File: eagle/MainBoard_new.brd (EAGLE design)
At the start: 62 parts, among them T1 BC847, U1 STM32F10XRXT6, U2 MPL115A, Y1 8MHz, Y2 32.768kHz

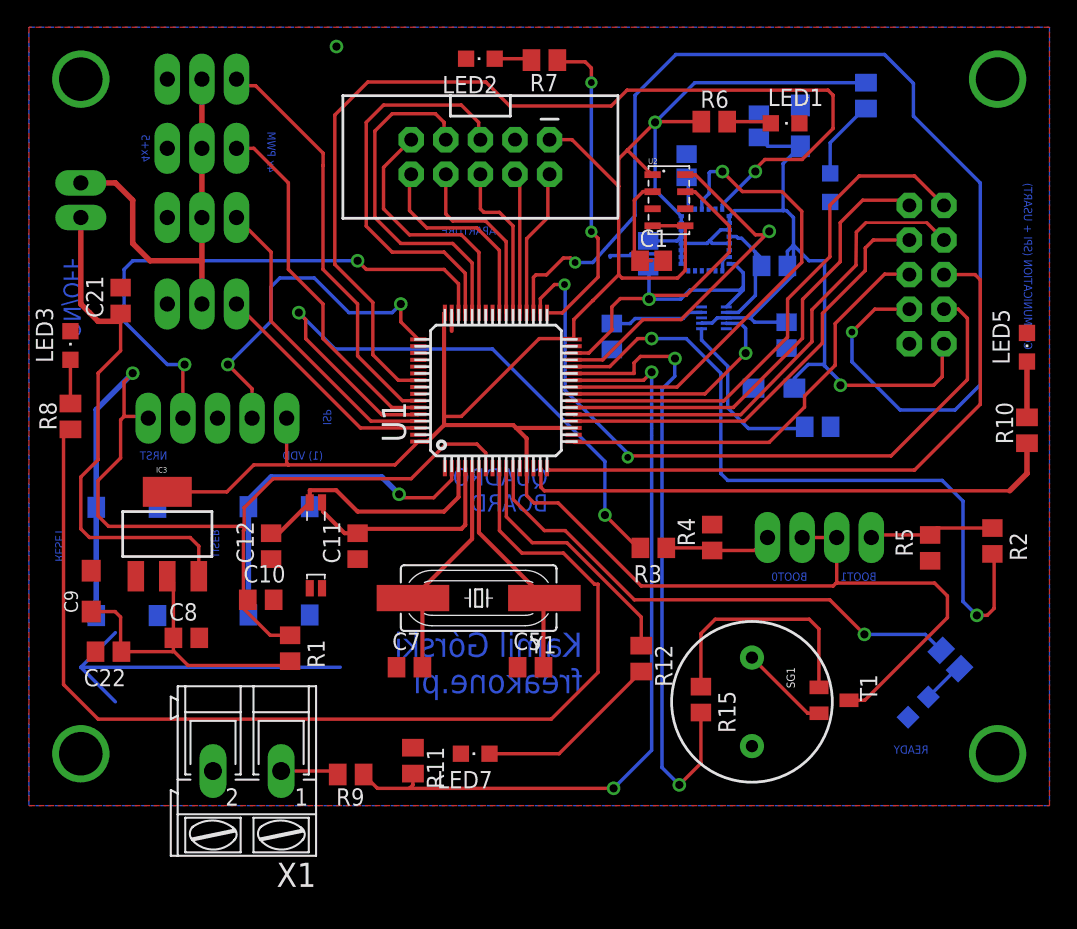
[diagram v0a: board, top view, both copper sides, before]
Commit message: likwidacja zbetnych przelotek do satlandu
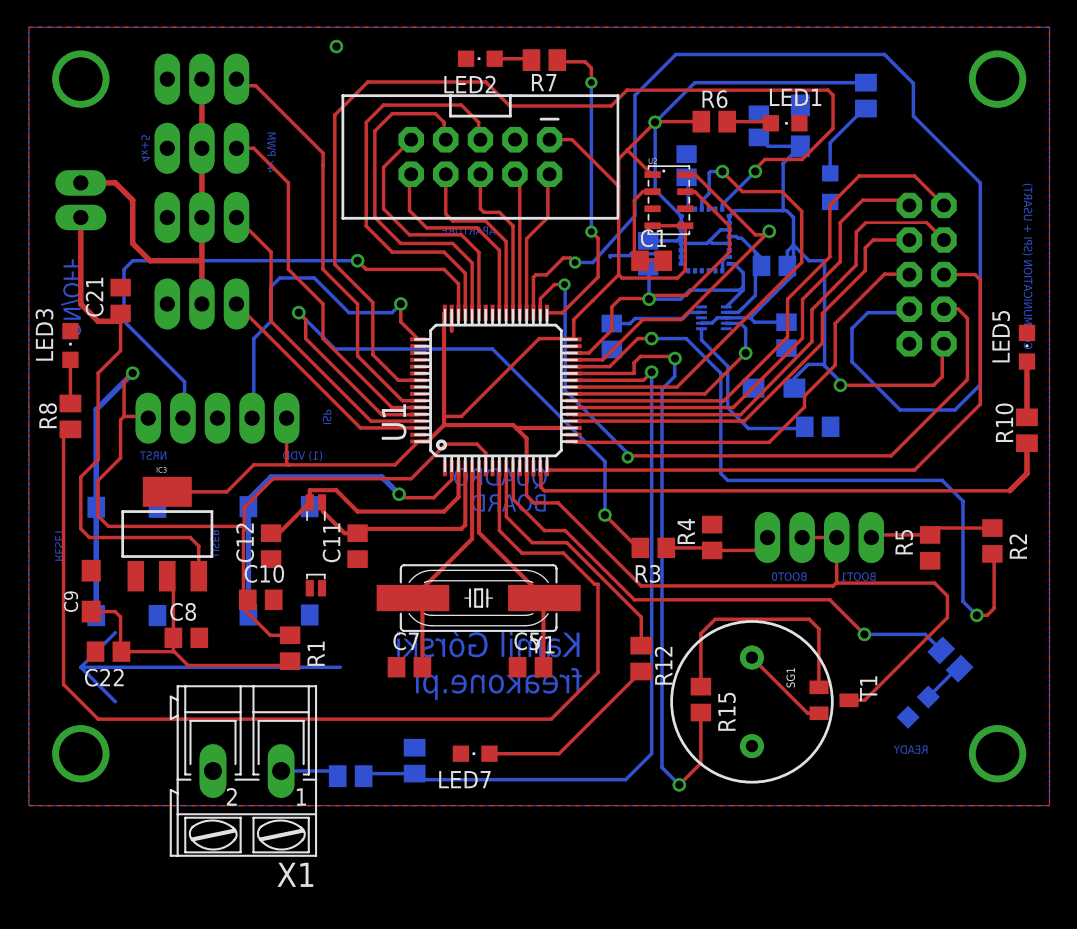
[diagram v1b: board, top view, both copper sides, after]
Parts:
- moved R11 0.13 mm to (18.2, 5.84), flipped to the bottom
- moved R9 0.13 mm to (13.5, 4.70), flipped to the bottom, turned to 0 degrees
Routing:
- net LIPO: track 57.7 -> 56.2 mm, vias 2 -> 1
- net SWCLK: track 25.9 -> 24.5 mm, vias 2 -> 1
- net SWDIO: track 41.2 -> 40.5 mm, vias 2 -> 1
- net OUT1: track 86.6 -> 86.8 mm, vias 2 -> 1
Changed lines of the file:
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@@
 <attribute name="OC_FARNELL" value="unknown" x="5.842" y="5.08" size="1.778" layer="27" rot="R180" display="off"/>
 </element>
-<element name="R9" library="resistor" package="M0805" value="" x="13.462" y="4.826" rot="R180"/>
-<element name="R11" library="resistor" package="M0805" value="" x="18.034" y="5.842" rot="R270"/>
+<element name="R9" library="resistor" package="M0805" value="" x="13.462" y="4.699" rot="MR0"/>
+<element name="R11" library="resistor" package="M0805" value="" x="18.161" y="5.842" rot="MR270"/>
 <element name="T1" library="transistor" package="SOT23" value="BC847" x="48.949871875" y="10.27251875" rot="R270"/>
 <element name="R15" library="rcl" package="R0805" value="" x="39.17856875" y="10.325953125" rot="R270"/>
@@
 <contactref element="U1" pad="46"/>
 <contactref element="JP1" pad="4"/>
-<wire x1="1.143" y1="30.988" x2="1.143" y2="34.798" width="0.254" layer="1"/>
-<wire x1="1.143" y1="34.798" x2="1.27" y2="34.925" width="0.254" layer="1"/>
-<via x="1.27" y="34.925" extent="1-16" drill="0.6" shape="square"/>
 <wire x1="21.38" y1="38.72" x2="21.38" y2="40.85" width="0.254" layer="1"/>
 <wire x1="21.38" y1="40.85" x2="20.32" y2="41.91" width="0.254" layer="1"/>
@@
 <wire x1="14.605" y1="41.91" x2="13.97" y2="42.545" width="0.254" layer="1"/>
 <via x="13.97" y="42.545" extent="1-16" drill="0.6" shape="square"/>
-<wire x1="1.27" y1="34.925" x2="0" y2="34.925" width="0.254" layer="16"/>
-<wire x1="0" y1="34.925" x2="-3.175" y2="38.1" width="0.254" layer="16"/>
+<wire x1="1.27" y1="33.655" x2="-3.175" y2="38.1" width="0.254" layer="16"/>
 <wire x1="-3.175" y1="38.1" x2="-3.175" y2="41.91" width="0.254" layer="16"/>
 <wire x1="-3.175" y1="41.91" x2="-2.54" y2="42.545" width="0.254" layer="16"/>
 <wire x1="-2.54" y1="42.545" x2="13.97" y2="42.545" width="0.254" layer="16"/>
+<wire x1="1.27" y1="33.655" x2="1.27" y2="31.115" width="0.254" layer="16"/>
+<wire x1="1.27" y1="31.115" x2="1.143" y2="30.988" width="0.254" layer="16"/>
 </signal>
 <signal name="SWCLK">
 <contactref element="U1" pad="49"/>
 <contactref element="JP1" pad="2"/>
-<wire x1="6.223" y1="30.988" x2="6.223" y2="33.147" width="0.254" layer="1"/>
-<wire x1="6.223" y1="33.147" x2="4.445" y2="34.925" width="0.254" layer="1"/>
-<via x="4.445" y="34.925" extent="1-16" drill="0.6" shape="square"/>
 <wire x1="13.335" y1="38.735" x2="16.51" y2="38.735" width="0.254" layer="16"/>
 <wire x1="16.51" y1="38.735" x2="17.145" y2="39.37" width="0.254" layer="16"/>
@@
 <wire x1="17.145" y1="39.37" x2="17.145" y2="38.055" width="0.254" layer="1"/>
 <wire x1="17.145" y1="38.055" x2="18.43" y2="36.77" width="0.254" layer="1"/>
-<wire x1="4.445" y1="34.925" x2="7.62" y2="38.1" width="0.254" layer="16"/>
+<wire x1="6.35" y1="36.83" x2="7.62" y2="38.1" width="0.254" layer="16"/>
 <wire x1="7.62" y1="38.1" x2="7.62" y2="40.64" width="0.254" layer="16"/>
 <wire x1="7.62" y1="40.64" x2="8.255" y2="41.275" width="0.254" layer="16"/>
 <wire x1="8.255" y1="41.275" x2="10.795" y2="41.275" width="0.254" layer="16"/>
 <wire x1="10.795" y1="41.275" x2="13.335" y2="38.735" width="0.254" layer="16"/>
+<wire x1="6.223" y1="30.988" x2="6.35" y2="30.988" width="0.254" layer="16"/>
+<wire x1="6.35" y1="30.988" x2="6.35" y2="36.83" width="0.254" layer="16"/>
 </signal>
 <signal name="V_BATT">
@@
 <contactref element="X1" pad="1"/>
 <contactref element="R9" pad="2"/>
-<wire x1="8.3566" y1="5.08" x2="12.258" y2="5.08" width="0.254" layer="1"/>
-<wire x1="12.258" y1="5.08" x2="12.512" y2="4.826" width="0.254" layer="1"/>
+<wire x1="12.258" y1="5.08" x2="12.512" y2="4.699" width="0.254" layer="16"/>
+<wire x1="12.258" y1="5.08" x2="8.3566" y2="5.08" width="0.254" layer="16"/>
 </signal>
 <signal name="LIPO">
@@
 <contactref element="U1" pad="26"/>
 <via x="35.56" y="34.36589375" extent="1-16" drill="0.6" shape="square"/>
-<wire x1="35.56" y1="30.226" x2="35.56" y2="29.71018125" width="0.254" layer="16"/>
-<wire x1="35.56" y1="29.71018125" x2="35.56" y2="6.604" width="0.254" layer="16"/>
-<wire x1="35.56" y1="6.604" x2="32.766" y2="3.81" width="0.254" layer="16"/>
-<via x="32.766" y="3.81" extent="1-16" drill="0.6" shape="square"/>
-<wire x1="32.766" y1="3.81" x2="17.78" y2="3.81" width="0.254" layer="1"/>
-<wire x1="17.78" y1="3.81" x2="15.428" y2="3.81" width="0.254" layer="1"/>
-<wire x1="15.428" y1="3.81" x2="14.412" y2="4.826" width="0.254" layer="1"/>
-<wire x1="18.034" y1="4.892" x2="18.034" y2="4.064" width="0.254" layer="1"/>
-<wire x1="18.034" y1="4.064" x2="17.78" y2="3.81" width="0.254" layer="1"/>
-<wire x1="35.56" y1="34.36589375" x2="35.56" y2="30.226" width="0.254" layer="16"/>
+<wire x1="35.56" y1="34.36589375" x2="35.56" y2="6.35" width="0.254" layer="16"/>
 <wire x1="29.83" y1="33.77" x2="34.96410625" y2="33.77" width="0.254" layer="1"/>
 <wire x1="34.96410625" y1="33.77" x2="35.56" y2="34.36589375" width="0.254" layer="1"/>
+<wire x1="35.56" y1="6.35" x2="33.655" y2="4.445" width="0.254" layer="16"/>
+<wire x1="33.655" y1="4.445" x2="18.608" y2="4.445" width="0.254" layer="16"/>
+<wire x1="18.608" y1="4.445" x2="18.161" y2="4.892" width="0.254" layer="16"/>
+<wire x1="18.161" y1="4.892" x2="14.605" y2="4.892" width="0.254" layer="16"/>
+<wire x1="14.605" y1="4.892" x2="14.412" y2="4.699" width="0.254" layer="16"/>
 </signal>
 <signal name="BUZZ">
@@
 <wire x1="31.23834375" y1="42.415703125" x2="34.34323125" y2="45.8634875" width="0.254" layer="16"/>
 <wire x1="34.34323125" y1="45.8634875" x2="34.34323125" y2="54.69315625" width="0.254" layer="16"/>
-<wire x1="54.483" y1="38.989" x2="51.94404375" y2="38.989" width="0.254" layer="1"/>
-<wire x1="51.94404375" y1="38.989" x2="50.26686875" y2="37.311825" width="0.254" layer="1"/>
-<via x="50.26686875" y="37.311825" extent="1-16" drill="0.5" shape="square"/>
-<wire x1="50.26686875" y1="37.311825" x2="50.26686875" y2="35.129590625" width="0.254" layer="16"/>
 <wire x1="50.26686875" y1="35.129590625" x2="53.80591875" y2="31.590540625" width="0.254" layer="16"/>
 <wire x1="53.80591875" y1="31.590540625" x2="57.83816875" y2="31.590540625" width="0.254" layer="16"/>
@@
 <wire x1="54.782240625" y1="55.565090625" x2="54.782240625" y2="53.167759375" width="0.254" layer="16"/>
 <wire x1="54.782240625" y1="53.167759375" x2="59.69" y2="48.26" width="0.254" layer="16"/>
+<wire x1="50.26686875" y1="35.129590625" x2="50.26686875" y2="37.56686875" width="0.254" layer="16"/>
+<wire x1="50.26686875" y1="37.56686875" x2="51.435" y2="38.735" width="0.254" layer="16"/>
+<wire x1="51.435" y1="38.735" x2="54.229" y2="38.735" width="0.254" layer="16"/>
+<wire x1="54.229" y1="38.735" x2="54.483" y2="38.989" width="0.254" layer="16"/>
 </signal>
 <signal name="OUT2">
